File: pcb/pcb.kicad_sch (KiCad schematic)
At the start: 19 parts, among them CN1 1x4, CN10 1x2, CN11 1x2, CN12 1x8, CN2 1x8, CN3 1x8, CN4 1x8, CN5 1x4, CN6 1x2, CN7 1x2, CN8 1x8, SW3 219-3LPST

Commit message: worked on layout
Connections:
- net Input  buffers/raw_1: now also CN8.1; no longer CN8.8
- net Input  buffers/raw_2: now also CN8.2; no longer CN8.7
- net Input  buffers/raw_3: now also CN8.3; no longer CN8.6
- net Input  buffers/raw_4: now also CN8.4; no longer CN8.5
- net Input  buffers/raw_5: now also CN8.5; no longer CN8.4
- net Input  buffers/raw_6: now also CN8.6; no longer CN8.3
- net Input  buffers/raw_7: now also CN8.7; no longer CN8.2
- net Input  buffers/raw_8: now also CN8.8; no longer CN8.1
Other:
- moved on the sheet: CN12, CN8
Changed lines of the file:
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@@
 	(symbol
 		(lib_id "pin_headers:1x8")
-		(at 71.12 129.54 180)
+		(at 71.12 127 0)
+		(mirror y)
 		(unit 1)
 		(exclude_from_sim no)
@@
 		(dnp no)
 		(property "Reference" "CN8"
-			(at 68.58 139.7 0)
+			(at 68.58 116.84 0)
 			(effects
 				(font
@@
 		)
 		(property "Value" "1x8"
-			(at 71.12 139.7 0)
+			(at 71.12 116.84 0)
 			(effects
 				(font
@@
 		)
 		(property "Footprint" "pin_headers:1x8"
-			(at 71.12 137.16 0)
-			(effects
-				(font
-					(size 1.27 1.27)
-				)
-				(hide yes)
-			)
-		)
-		(property "Datasheet" ""
-			(at 71.12 132.08 0)
-			(effects
-				(font
-					(size 1.27 1.27)
-				)
-				(hide yes)
-			)
-		)
-		(property "Description" ""
-			(at 71.12 129.54 0)
+			(at 71.12 119.38 0)
+			(effects
+				(font
+					(size 1.27 1.27)
+				)
+				(hide yes)
+			)
+		)
+		(property "Datasheet" ""
+			(at 71.12 124.46 0)
+			(effects
+				(font
+					(size 1.27 1.27)
+				)
+				(hide yes)
+			)
+		)
+		(property "Description" ""
+			(at 71.12 127 0)
 			(effects
 				(font
@@
 	(symbol
 		(lib_id "pin_headers:1x8")
-		(at 58.42 129.54 180)
+		(at 58.42 127 0)
+		(mirror y)
 		(unit 1)
 		(exclude_from_sim no)
@@
 		(dnp no)
 		(property "Reference" "CN12"
-			(at 55.88 139.7 0)
+			(at 55.88 116.84 0)
 			(effects
 				(font
@@
 		)
 		(property "Value" "1x8"
-			(at 58.42 139.7 0)
+			(at 58.42 116.84 0)
 			(effects
 				(font
@@
 		)
 		(property "Footprint" "pin_headers:1x8"
-			(at 58.42 137.16 0)
-			(effects
-				(font
-					(size 1.27 1.27)
-				)
-				(hide yes)
-			)
-		)
-		(property "Datasheet" ""
-			(at 58.42 132.08 0)
-			(effects
-				(font
-					(size 1.27 1.27)
-				)
-				(hide yes)
-			)
-		)
-		(property "Description" ""
-			(at 58.42 129.54 0)
-			(effects
-				(font
+			(at 58.42 119.38 0)
+			(effects
+				(font
+					(size 1.27 1.27)
+				)
+				(hide yes)
+			)
+		)
+		(property "Datasheet" ""
+			(at 58.42 124.46 0)
+			(effects
+				(font
+					(size 1.27 1.27)
+				)
+				(hide yes)
+			)
+		)
+		(property "Description" ""
+			(at 58.42 127 0)
+			(effects
+				(font

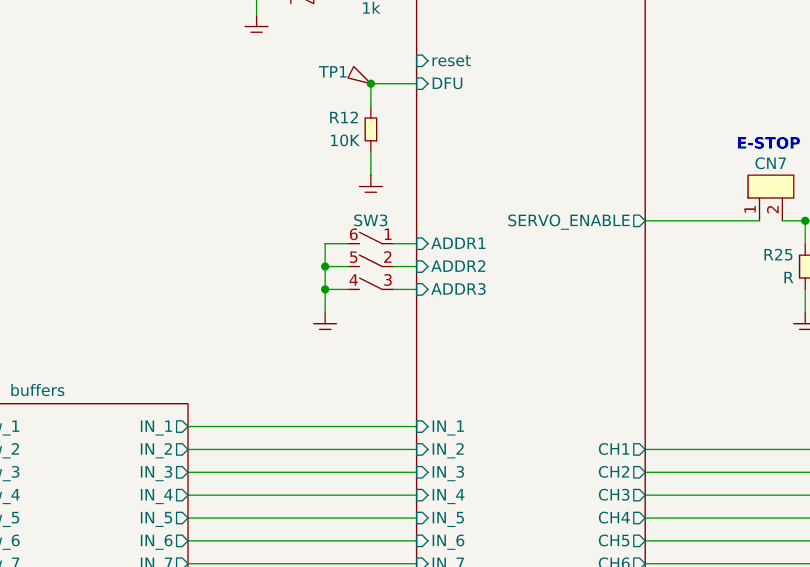
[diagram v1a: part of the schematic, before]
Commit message: changed dip switch to rotary type
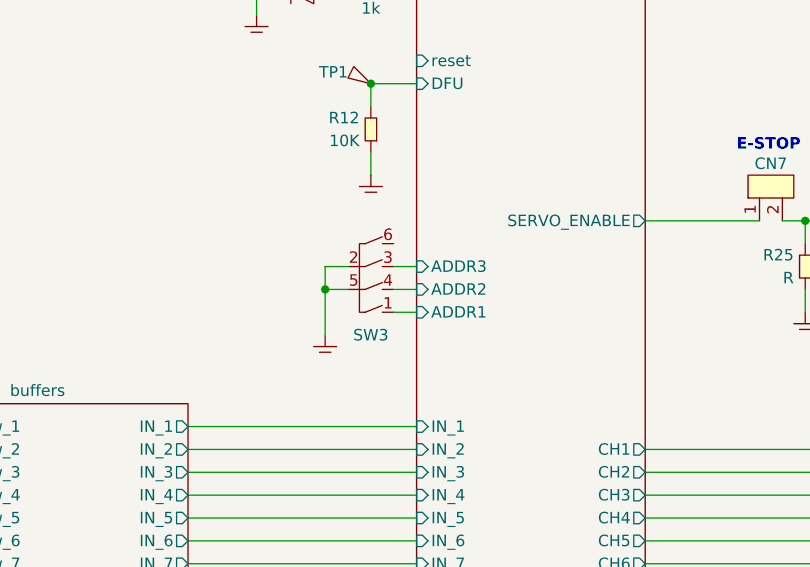
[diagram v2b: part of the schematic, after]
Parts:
- SW3: value 219-3LPST -> RD10RA8RTT; footprint buttons:219-3LPST -> buttons:RD10RA8RTT; symbol switches:219-3LPST -> switches:RD10RA8RTT; Digi-Key CT2193LPST-ND -> 2449-RD10RA8RTT-ND; MPN 219-3LPST -> RD10RA8RTT
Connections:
- net GND: now also SW3.2; no longer SW3.4, SW3.6
- net MCU/ADDR2: now also SW3.4; no longer SW3.2
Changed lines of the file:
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@@
 	)
 	(junction
-		(at 116.84 101.6)
+		(at 116.84 104.14)
 		(diameter 0)
 		(color 0 0 0 0)
@@
 	)
 	(junction
-		(at 116.84 104.14)
-		(diameter 0)
-		(color 0 0 0 0)
-	)
-	(junction
 		(at 231.14 129.54)
 		(diameter 0)
@@
 	(wire
 		(pts
-			(xy 116.84 101.6) (xy 119.38 101.6)
+			(xy 116.84 104.14) (xy 119.38 104.14)
 		)
 		(stroke
@@
 	(wire
 		(pts
-			(xy 116.84 101.6) (xy 116.84 99.06)
+			(xy 116.84 104.14) (xy 116.84 101.6)
 		)
 		(stroke
@@
 	(wire
 		(pts
-			(xy 124.46 99.06) (xy 127 99.06)
+			(xy 124.46 101.6) (xy 127 101.6)
 		)
 		(stroke
@@
 	(wire
 		(pts
-			(xy 116.84 99.06) (xy 119.38 99.06)
+			(xy 116.84 101.6) (xy 119.38 101.6)
 		)
 		(stroke
@@
 	(wire
 		(pts
-			(xy 124.46 104.14) (xy 127 104.14)
+			(xy 124.46 106.68) (xy 127 106.68)
 		)
 		(stroke
@@
 	(wire
 		(pts
-			(xy 116.84 104.14) (xy 116.84 101.6)
-		)
-		(stroke
-			(width 0)
-			(type default)
-		)
-	)
-	(wire
-		(pts
-			(xy 116.84 104.14) (xy 119.38 104.14)
-		)
-		(stroke
-			(width 0)
-			(type default)
-		)
-	)
-	(wire
-		(pts
 			(xy 177.8 96.52) (xy 180.34 96.52)
 		)
@@
 	(wire
 		(pts
-			(xy 116.84 106.68) (xy 116.84 104.14)
+			(xy 116.84 104.14) (xy 116.84 109.22)
 		)
 		(stroke
@@
 	(wire
 		(pts
-			(xy 124.46 101.6) (xy 127 101.6)
+			(xy 124.46 104.14) (xy 127 104.14)
 		)
 		(stroke
@@
 	(symbol
 		(lib_id "generic:GND")
-		(at 116.84 106.68 0)
+		(at 116.84 109.22 0)
 		(unit 1)
 		(exclude_from_sim no)
@@
 		(fields_autoplaced yes)
 		(property "Reference" "#GND01"
-			(at 120.65 105.41 0)
+			(at 120.65 107.95 0)
 			(effects
 				(font
@@
 		)
 		(property "Value" "GND"
-			(at 120.65 106.68 0)
+			(at 120.65 109.22 0)
 			(effects
 				(font
@@
 		)
 		(property "Footprint" ""
-			(at 116.84 106.68 0)
+			(at 116.84 109.22 0)
 			(effects
 				(font
@@
 		)
 		(property "Datasheet" ""
-			(at 116.84 106.68 0)
+			(at 116.84 109.22 0)
 			(effects
 				(font
@@
 		)
 		(property "Description" ""
-			(at 116.84 106.68 0)
+			(at 116.84 109.22 0)
 			(effects
 				(font
@@
 	)
 	(symbol
-		(lib_id "switches:219-3LPST")
-		(at 121.92 99.06 0)
-		(mirror y)
+		(lib_id "switches:RD10RA8RTT")
+		(at 121.92 101.6 0)
 		(unit 1)
 		(exclude_from_sim no)
@@
 		(on_board yes)
 		(dnp no)
-		(fields_autoplaced yes)
 		(property "Reference" "SW3"
-			(at 121.92 96.52 0)
+			(at 121.92 109.22 0)
 			(effects
 				(font
@@
 			)
 		)
-		(property "Value" "219-3LPST"
-			(at 121.92 92.71 0)
+		(property "Value" "RD10RA8RTT"
+			(at 121.92 95.25 0)
 			(effects
 				(font
@@
 			)
 		)
-		(property "Footprint" "buttons:219-3LPST"
-			(at 121.92 106.68 0)
+		(property "Footprint" "buttons:RD10RA8RTT"
+			(at 121.92 109.22 0)
 			(effects
 				(font
@@
 			)
 		)
-		(property "Datasheet" "https://www.ctscorp.com/Files/DataSheets/Switches/DIP-Switches/CTS-Switches-DIP-219-Series-Datasheet.pdf"
-			(at 123.19 91.44 0)
+		(property "Datasheet" "https://www.citrelay.com/Catalog%20Pages/SwitchCatalog/RD10.pdf"
+			(at 120.65 93.98 0)
 			(effects
 				(font
@@
 			)
 		)
-		(property "Description" ""
-			(at 121.92 99.06 0)
+		(property "Description" "rotary  DIP Switch"
+			(at 122.936 96.266 0)
 			(effects
 				(font
@@
 			)
 		)
-		(property "Digi-Key" "CT2193LPST-ND"
-			(at 121.92 92.71 0)
+		(property "Digi-Key" "2449-RD10RA8RTT-ND"
+			(at 121.92 95.25 0)
 			(effects
 				(font
@@
 			)
 		)
-		(property "MPN" "219-3LPST"
-			(at 121.92 106.68 0)
+		(property "MPN" "RD10RA8RTT"
+			(at 121.92 109.22 0)
 			(effects
 				(font
@@
 		)
 		(pin "ADDR3" input
-			(at 127 104.14 180)
+			(at 127 101.6 180)
 			(effects
 				(font
@@
 		)
 		(pin "ADDR2" input
-			(at 127 101.6 180)
+			(at 127 104.14 180)
 			(effects
 				(font
@@
 		)
 		(pin "ADDR1" input
-			(at 127 99.06 180)
+			(at 127 106.68 180)
 			(effects
 				(font

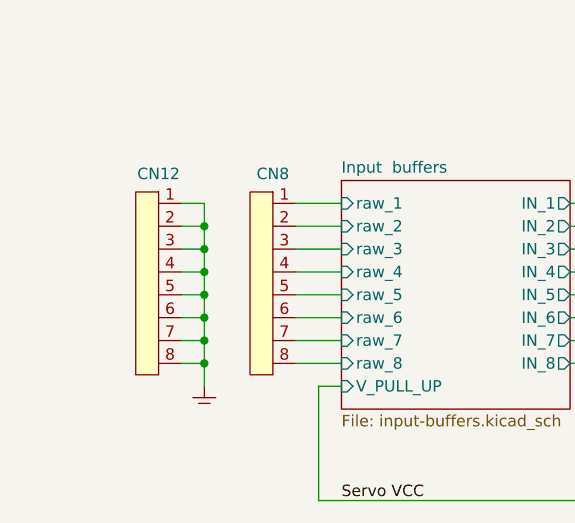
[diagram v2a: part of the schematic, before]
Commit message: worked on layout, added power to sensor connectors
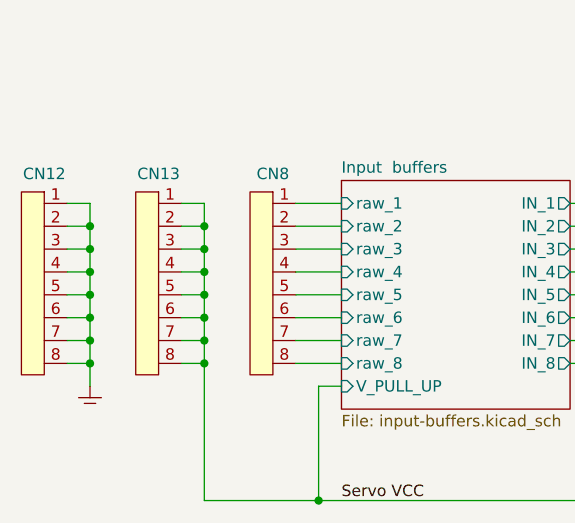
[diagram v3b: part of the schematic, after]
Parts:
- added CN13: 1x8, pin_headers:1x8, symbol pin_headers:1x8
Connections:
- net Servo VCC: now also CN13.1, CN13.2, CN13.3, CN13.4, CN13.5, CN13.6, CN13.7, CN13.8
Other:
- moved on the sheet: CN12
